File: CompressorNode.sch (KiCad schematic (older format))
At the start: 33 parts, among them J1 EXT1, J10 Screw_Terminal_01x03, J11 Screw_Terminal_01x02, J12 Screw_Terminal_01x03, J13 Screw_Terminal_01x04, J2 Screw_Terminal_01x04, J3 Screw_Terminal_01x03, J4 EXT2, J5 Screw_Terminal_01x02, J6 Screw_Terminal_01x02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

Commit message: Adjusted R2 and R4 to 220R (instead of 1k)
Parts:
- R2, R4: value 1k -> 220R
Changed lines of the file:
@@
 Title "CompressorNode"
 Date "2020-03-24"
-Rev "V0.2 Concept"
+Rev "V0.3 Concept"
 Comp "MakerSpace Leiden"
 Comment1 "Getekend door Hans Beerman"
@@
 P 2750 6500
 F 0 "R2" V 2850 6500 50  0000 C CNN
-F 1 "1k" V 2750 6500 50  0000 C CNN
+F 1 "220R" V 2750 6500 50  0000 C CNN
 F 2 "Resistor_THT:R_Axial_DIN0207_L6.3mm_D2.5mm_P7.62mm_Horizontal" V 2680 6500 50  0001 C CNN
 F 3 "~" H 2750 6500 50  0001 C CNN
@@
 P 5050 6500
 F 0 "R4" V 5150 6500 50  0000 C CNN
-F 1 "1k" V 5050 6500 50  0000 C CNN
+F 1 "220R" V 5050 6500 50  0000 C CNN
 F 2 "Resistor_THT:R_Axial_DIN0207_L6.3mm_D2.5mm_P7.62mm_Horizontal" V 4980 6500 50  0001 C CNN
 F 3 "~" H 5050 6500 50  0001 C CNN

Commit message: PCB designed
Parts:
- OK1: footprint PC814:DIL04 -> Package_DIP:DIP-4_W7.62mm
- R8, R9: footprint Resistor_THT:R_Axial_DIN0207_L6.3mm_D2.5mm_P7.62mm_Horizontal -> Resistor_THT:R_Axial_DIN0614_L14.3mm_D5.7mm_P20.32mm_Horizontal
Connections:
- net GND: now also OK1.2 (AC2); no longer OK1.3 (E)
- net GPI36_U1RXD: now also OK1.1 (AC1); no longer OK1.4 (C)
- net at J10.1 (Pin_1): now also K1.3; no longer K1.4
- net at J10.3 (Pin_3): now also K1.4; no longer K1.3
- net at R8.2: now also OK1.4 (C); no longer OK1.1 (AC1)
- net at R9.2: now also OK1.3 (E); no longer OK1.2 (AC2)
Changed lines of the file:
@@
 Sheet 1 1
 Title "CompressorNode"
-Date "2020-03-24"
-Rev "V0.3 Concept"
+Date "2020-03-25"
+Rev "V0.4 Concept"
 Comp "MakerSpace Leiden"
 Comment1 "Getekend door Hans Beerman"
@@
 F 3 "~" H 8200 1200 50  0001 C CNN
 	1    8200 1200
-	1    0    0    -1
+	1    0    0    1
 $EndComp
 Wire Wire Line
@@
 Wire Wire Line
 	6350 850  6350 900
-$Comp
-L PC814:PC814 OK1
-U 1 1 5E862303
-P 6900 5400
-F 0 "OK1" H 6950 5770 50  0000 C CNN
-F 1 "PC814" H 6950 5679 50  0000 C CNN
-F 2 "PC814:DIL04" H 6900 5400 50  0001 L BNN
-F 3 "" H 6900 5400 50  0001 L BNN
-F 4 "unknown" H 6900 5400 50  0001 L BNN "Field4"
-F 5 "9707662" H 6900 5400 50  0001 L BNN "Field5"
-F 6 "" H 6900 5400 50  0001 L BNN "Field6"
-	1    6900 5400
-	-1   0    0    -1
-$EndComp
 $Comp
 L Connector:Screw_Terminal_01x02 J11
@@
 F 0 "R9" V 7750 5500 50  0000 C CNN
 F 1 "220k" V 7650 5500 50  0000 C CNN
-F 2 "Resistor_THT:R_Axial_DIN0207_L6.3mm_D2.5mm_P7.62mm_Horizontal" V 7580 5500 50  0001 C CNN
+F 2 "Resistor_THT:R_Axial_DIN0614_L14.3mm_D5.7mm_P20.32mm_Horizontal" V 7580 5500 50  0001 C CNN
 F 3 "~" H 7650 5500 50  0001 C CNN
 	1    7650 5500
@@
 F 0 "R8" V 7750 5300 50  0000 C CNN
 F 1 "220k" V 7650 5300 50  0000 C CNN
-F 2 "Resistor_THT:R_Axial_DIN0207_L6.3mm_D2.5mm_P7.62mm_Horizontal" V 7580 5300 50  0001 C CNN
+F 2 "Resistor_THT:R_Axial_DIN0614_L14.3mm_D5.7mm_P20.32mm_Horizontal" V 7580 5300 50  0001 C CNN
 F 3 "~" H 7650 5300 50  0001 C CNN
 	1    7650 5300
@@
 Text Notes 8300 1135 0    49   ~ 0
 NC
-Text Notes 8300 1240 0    49   ~ 0
+Text Notes 8300 1350 0    49   ~ 0
 NO
-Text Notes 8300 1340 0    49   ~ 0
+Text Notes 8300 1250 0    49   ~ 0
 Common
 Text Notes 8300 5350 0    49   ~ 0
@@
 Wire Wire Line
 	2300 5150 3600 5150
+$Comp
+L PC814:PC814 OK1
+U 1 1 5E7B5CDC
+P 6800 5400
+F 0 "OK1" H 6850 5770 50  0000 C CNN
+F 1 "PC814" H 6850 5679 50  0000 C CNN
+F 2 "Package_DIP:DIP-4_W7.62mm" H 6800 5400 50  0001 L BNN
+F 3 "" H 6800 5400 50  0001 L BNN
+F 4 "unknown" H 6800 5400 50  0001 L BNN "Field4"
+F 5 "9707662" H 6800 5400 50  0001 L BNN "Field5"
+F 6 "" H 6800 5400 50  0001 L BNN "Field6"
+	1    6800 5400
+	1    0    0    -1
+$EndComp
 $EndSCHEMATC

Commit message: corrected the groundplane and som PCB lines to create more distance to the 230V components
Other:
- note added: "A"
- note added: "K"
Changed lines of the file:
@@
 Sheet 1 1
 Title "CompressorNode"
-Date "2020-03-25"
-Rev "V0.4 Concept"
+Date "2020-03-26"
+Rev "V0.5 Concept"
 Comp "MakerSpace Leiden"
 Comment1 "Getekend door Hans Beerman"
@@
 	1    0    0    -1
 $EndComp
+Text Notes 3050 6750 0    49   ~ 10
+A
+Text Notes 3050 6900 0    49   ~ 10
+K
+Text Notes 5350 6750 0    49   ~ 10
+A
+Text Notes 5350 6900 0    49   ~ 10
+K
 $EndSCHEMATC

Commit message: LED Resistnow 47R to increase current for high power LEDs
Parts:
- R2, R4: value 220R -> 47R
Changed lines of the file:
@@
 Sheet 1 1
 Title "CompressorNode"
-Date "2020-03-29"
-Rev "V0.7 Concept"
+Date "2020-03-30"
+Rev "V0.8 Concept"
 Comp "MakerSpace Leiden"
 Comment1 "Getekend door Hans Beerman"
@@
 P 2750 6500
 F 0 "R2" V 2850 6500 50  0000 C CNN
-F 1 "220R" V 2750 6500 50  0000 C CNN
+F 1 "47R" V 2750 6500 50  0000 C CNN
 F 2 "Resistor_THT:R_Axial_DIN0207_L6.3mm_D2.5mm_P7.62mm_Horizontal" V 2680 6500 50  0001 C CNN
 F 3 "~" H 2750 6500 50  0001 C CNN
@@
 P 5050 6500
 F 0 "R4" V 5150 6500 50  0000 C CNN
-F 1 "220R" V 5050 6500 50  0000 C CNN
+F 1 "47R" V 5050 6500 50  0000 C CNN
 F 2 "Resistor_THT:R_Axial_DIN0207_L6.3mm_D2.5mm_P7.62mm_Horizontal" V 4980 6500 50  0001 C CNN
 F 3 "~" H 5050 6500 50  0001 C CNN

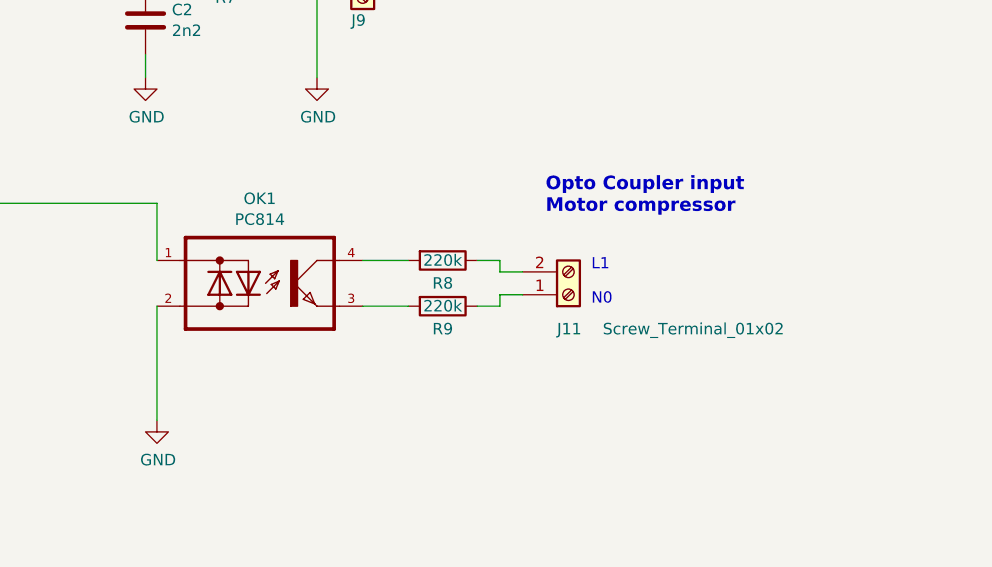
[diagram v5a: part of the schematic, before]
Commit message: Optocoupler was connected wrong
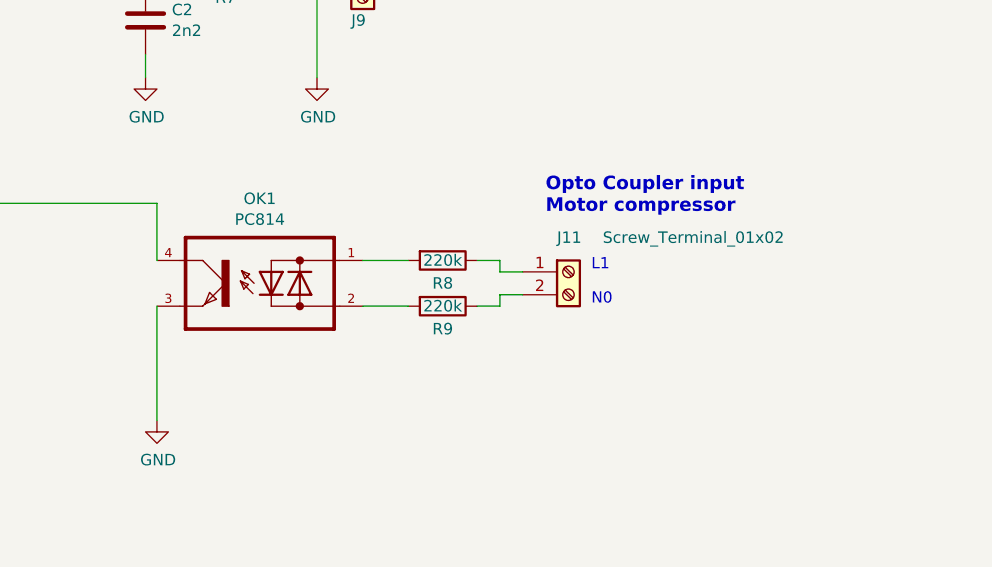
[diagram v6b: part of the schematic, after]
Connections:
- net GND: now also OK1.3 (E); no longer OK1.2 (AC2)
- net GPI36_U1RXD: now also OK1.4 (C); no longer OK1.1 (AC1)
- net at R9.2: now also OK1.2 (AC2); no longer OK1.3 (E)
- net at R8.2: now also OK1.1 (AC1); no longer OK1.4 (C)
- net at J11.1 (Pin_1): now also R8.1; no longer R9.1
- net at J11.2 (Pin_2): now also R9.1; no longer R8.1
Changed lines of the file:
@@
 Sheet 1 1
 Title "CompressorNode"
-Date "2020-03-30"
-Rev "V0.8 Concept"
+Date "2020-04-01"
+Rev "V0.9 Concept"
 Comp "MakerSpace Leiden"
 Comment1 "Getekend door Hans Beerman"
@@
 L Connector:Screw_Terminal_01x02 J11
 U 1 1 5E862309
-P 8200 5450
-F 0 "J11" H 8150 5600 50  0000 L CNN
-F 1 "Screw_Terminal_01x02" H 8350 5600 50  0000 L CNN
-F 2 "TerminalBlock_RND:TerminalBlock_RND_205-00287_1x02_P5.08mm_Horizontal" H 8200 5450 50  0001 C CNN
-F 3 "~" H 8200 5450 50  0001 C CNN
-	1    8200 5450
-	1    0    0    1
+P 8200 5350
+F 0 "J11" H 8150 5500 50  0000 L CNN
+F 1 "Screw_Terminal_01x02" H 8350 5500 50  0000 L CNN
+F 2 "TerminalBlock_RND:TerminalBlock_RND_205-00287_1x02_P5.08mm_Horizontal" H 8200 5350 50  0001 C CNN
+F 3 "~" H 8200 5350 50  0001 C CNN
+	1    8200 5350
+	1    0    0    -1
 $EndComp
 $Comp
@@
 L PC814:PC814 OK1
 U 1 1 5E7B5CDC
-P 6800 5400
-F 0 "OK1" H 6850 5770 50  0000 C CNN
-F 1 "PC814" H 6850 5679 50  0000 C CNN
-F 2 "Package_DIP:DIP-4_W7.62mm" H 6800 5400 50  0001 L BNN
-F 3 "" H 6800 5400 50  0001 L BNN
-F 4 "unknown" H 6800 5400 50  0001 L BNN "Field4"
-F 5 "9707662" H 6800 5400 50  0001 L BNN "Field5"
-F 6 "" H 6800 5400 50  0001 L BNN "Field6"
-	1    6800 5400
-	1    0    0    -1
+P 6900 5400
+F 0 "OK1" H 6950 5770 50  0000 C CNN
+F 1 "PC814" H 6950 5679 50  0000 C CNN
+F 2 "Package_DIP:DIP-4_W7.62mm" H 6900 5400 50  0001 L BNN
+F 3 "" H 6900 5400 50  0001 L BNN
+F 4 "unknown" H 6900 5400 50  0001 L BNN "Field4"
+F 5 "9707662" H 6900 5400 50  0001 L BNN "Field5"
+F 6 "" H 6900 5400 50  0001 L BNN "Field6"
+	1    6900 5400
+	-1   0    0    -1
 $EndComp
 Text Notes 3050 6750 0    49   ~ 10

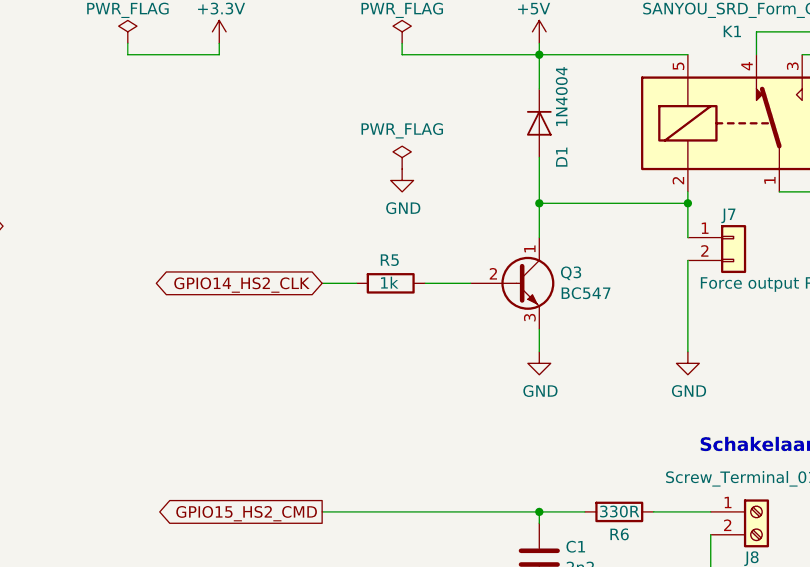
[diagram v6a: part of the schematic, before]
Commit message: R5 is now 150R because relais uses more current than expected
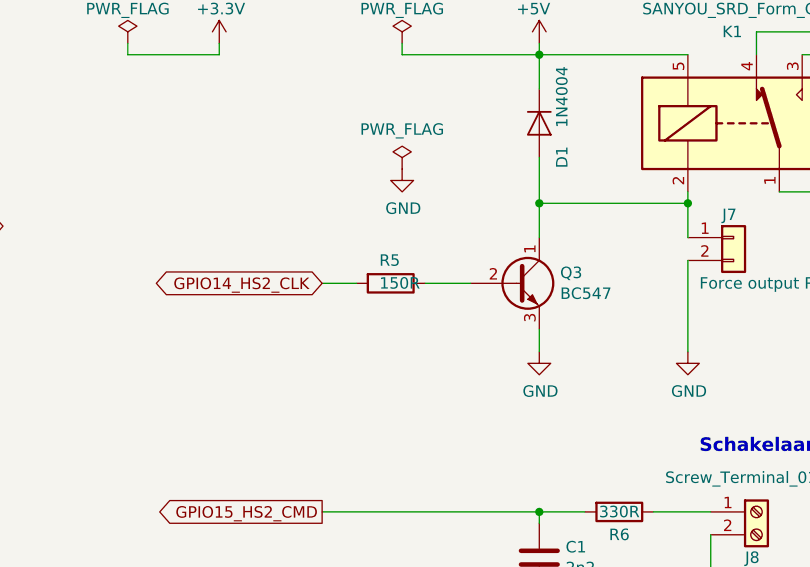
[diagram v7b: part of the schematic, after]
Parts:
- R5: value 1k -> 150R
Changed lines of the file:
@@
 Title "CompressorNode"
 Date "2020-04-01"
-Rev "V0.9 Concept"
+Rev "V0.10 Concept"
 Comp "MakerSpace Leiden"
 Comment1 "Getekend door Hans Beerman"
@@
 P 5700 1900
 F 0 "R5" V 5600 1850 50  0000 L CNN
-F 1 "1k" V 5700 1850 50  0000 L CNN
+F 1 "150R" V 5700 1850 50  0000 L CNN
 F 2 "Resistor_THT:R_Axial_DIN0207_L6.3mm_D2.5mm_P7.62mm_Horizontal" V 5630 1900 50  0001 C CNN
 F 3 "~" H 5700 1900 50  0001 C CNN

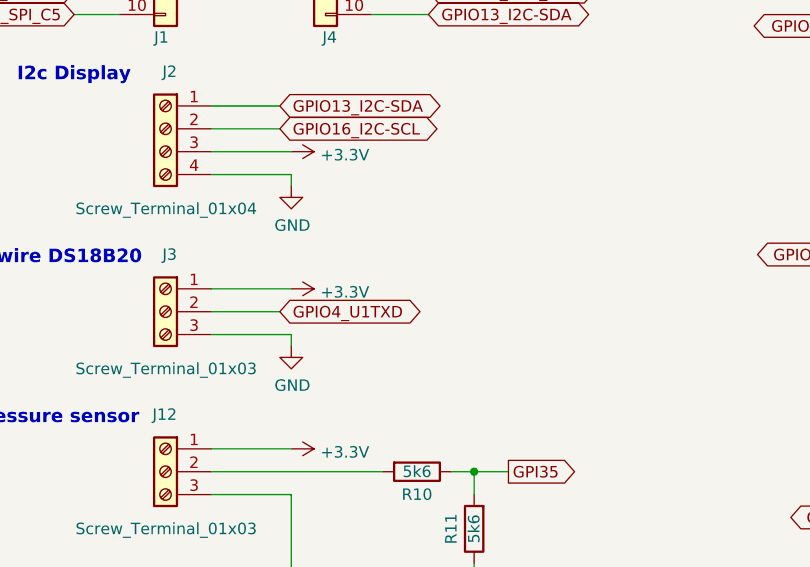
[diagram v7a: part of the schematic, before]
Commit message: resistor 4k7 added for DS18B20 temperature sensor
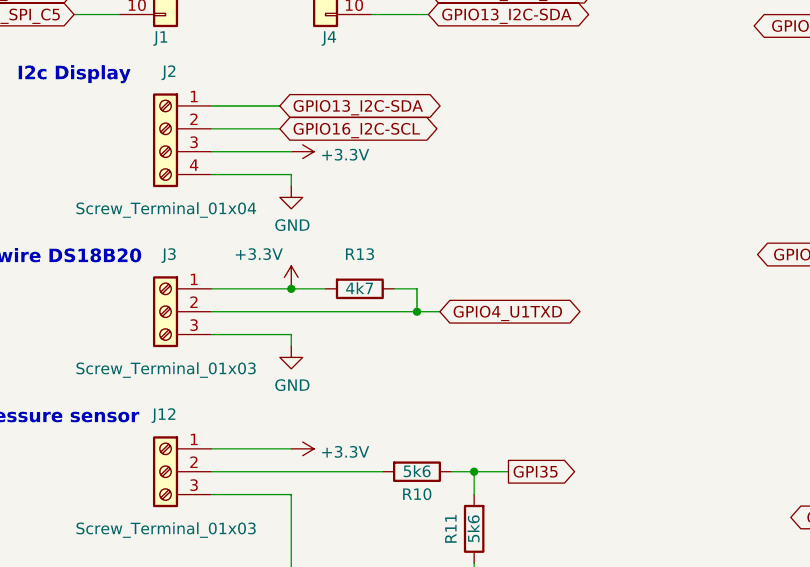
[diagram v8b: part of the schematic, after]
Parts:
- added R13: 4k7, Resistor_THT:R_Axial_DIN0207_L6.3mm_D2.5mm_P7.62mm_Horizontal, symbol Device:R
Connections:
- net +3V3: now also R13.2
- net GPIO4_U1TXD: now also R13.1
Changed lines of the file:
@@
 Sheet 1 1
 Title "CompressorNode"
-Date "2020-04-01"
-Rev "V0.10 Concept"
+Date "2020-04-02"
+Rev "V0.11 Concept"
 Comp "MakerSpace Leiden"
 Comment1 "Getekend door Hans Beerman"
@@
 	-1   0    0    -1
 $EndComp
-Text GLabel 2600 3150 2    50   BiDi ~ 0
+Text GLabel 3300 3150 2    50   BiDi ~ 0
 GPIO4_U1TXD
-Wire Wire Line
-	2300 3150 2600 3150
 $Comp
 L power:GND #PWR07
@@
 P 2650 3050
 F 0 "#PWR06" H 2650 2900 50  0001 C CNN
-F 1 "+3.3V" V 2665 3178 50  0000 L CNN
+F 1 "+3.3V" H 2400 3200 50  0000 L CNN
 F 2 "" H 2650 3050 50  0001 C CNN
 F 3 "" H 2650 3050 50  0001 C CNN
 	1    2650 3050
-	0    1    1    0
+	1    0    0    -1
 $EndComp
 Wire Wire Line
@@
 Text Notes 5350 6900 0    49   ~ 10
 K
+$Comp
+L Device:R R13
+U 1 1 5E870D9B
+P 2950 3050
+F 0 "R13" V 2800 3050 50  0000 C CNN
+F 1 "4k7" V 2950 3050 50  0000 C CNN
+F 2 "Resistor_THT:R_Axial_DIN0207_L6.3mm_D2.5mm_P7.62mm_Horizontal" V 2880 3050 50  0001 C CNN
+F 3 "~" H 2950 3050 50  0001 C CNN
+	1    2950 3050
+	0    1    1    0
+$EndComp
+Wire Wire Line
+	2650 3050 2800 3050
+Connection ~ 2650 3050
+Wire Wire Line
+	2300 3150 3200 3150
+Wire Wire Line
+	3100 3050 3200 3050
+Wire Wire Line
+	3200 3050 3200 3150
+Connection ~ 3200 3150
+Wire Wire Line
+	3200 3150 3300 3150
 $EndSCHEMATC
